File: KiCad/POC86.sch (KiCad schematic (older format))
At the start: 4 parts, among them J1 Conn_2Rows-86Pins_even_odd, J2 Conn_2Rows-86Pins_even_odd, J3 Conn_2Rows-86Pins_even_odd

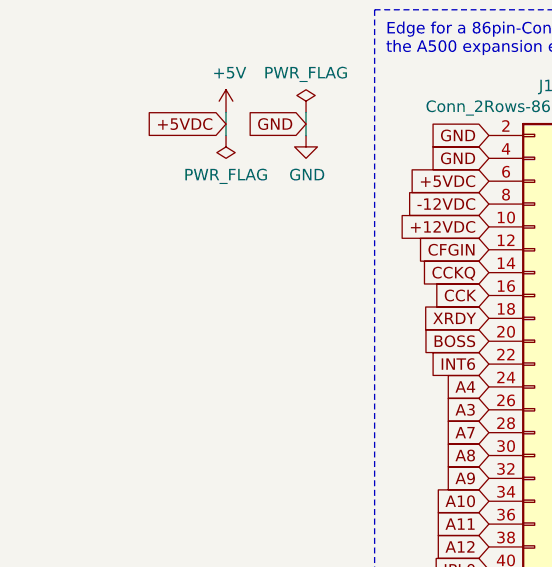
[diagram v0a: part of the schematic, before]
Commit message: added C1,C2 radial THT-capacitors for +5V-rail
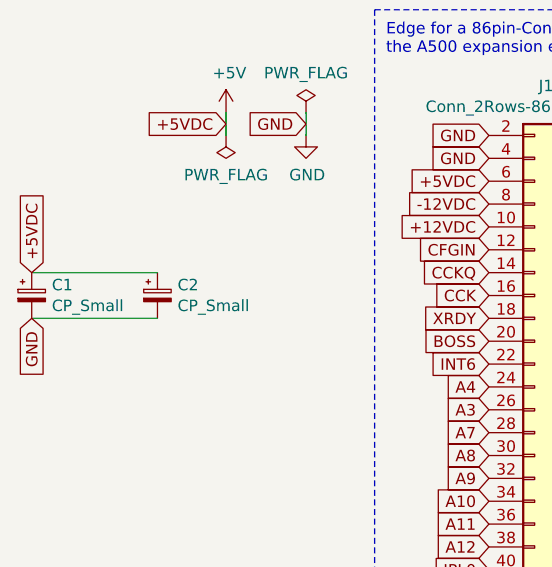
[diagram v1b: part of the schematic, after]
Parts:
- added C1, C2: CP_Small, Capacitor_THT:CP_Radial_D5.0mm_P2.50mm, symbol Device:CP_Small
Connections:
- net +5V: now also C1.1, C2.1
- net GND: now also C1.2, C2.2
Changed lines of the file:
@@
 Text Notes 5500 700  0    50   ~ 0
 New (Pass-through) expansion edge
+$Comp
+L Device:CP_Small C2
+U 1 1 628051CA
+P 1350 2250
+F 0 "C2" H 1438 2296 50  0000 L CNN
+F 1 "CP_Small" H 1438 2205 50  0000 L CNN
+F 2 "Capacitor_THT:CP_Radial_D5.0mm_P2.50mm" H 1350 2250 50  0001 C CNN
+F 3 "~" H 1350 2250 50  0001 C CNN
+	1    1350 2250
+	1    0    0    -1
+$EndComp
+$Comp
+L Device:CP_Small C1
+U 1 1 62805DF5
+P 800 2250
+F 0 "C1" H 888 2296 50  0000 L CNN
+F 1 "CP_Small" H 888 2205 50  0000 L CNN
+F 2 "Capacitor_THT:CP_Radial_D5.0mm_P2.50mm" H 800 2250 50  0001 C CNN
+F 3 "~" H 800 2250 50  0001 C CNN
+	1    800  2250
+	1    0    0    -1
+$EndComp
+Text GLabel 800  2150 1    50   Input ~ 0
++5VDC
+Wire Wire Line
+	800  2150 1350 2150
+Text GLabel 800  2350 3    50   Input ~ 0
+GND
+Wire Wire Line
+	800  2350 1350 2350
 $EndSCHEMATC

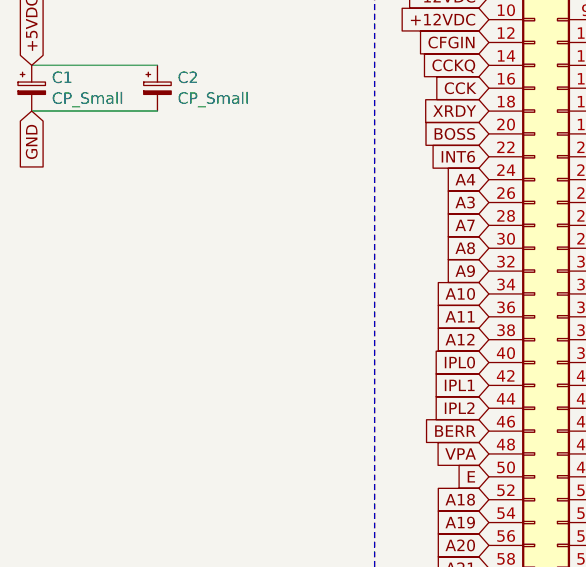
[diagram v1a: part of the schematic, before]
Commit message: added J4-pin on CFGIN-line to easily patch through this signal to J3-edge if J2-slot is empty
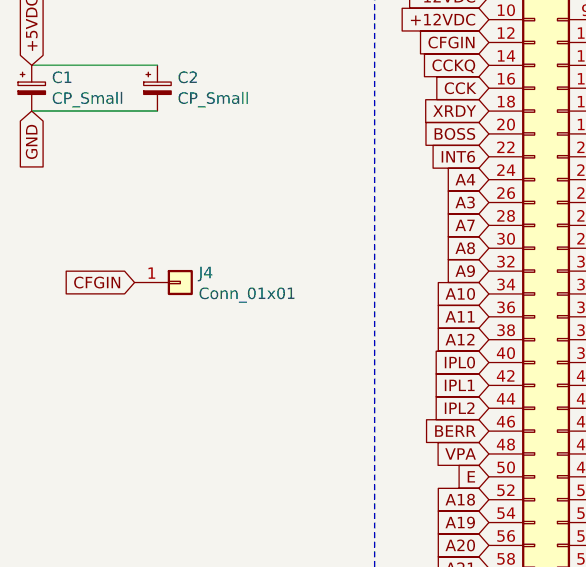
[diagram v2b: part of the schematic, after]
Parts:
- added J4: Conn_01x01, Connector_PinHeader_2.54mm:PinHeader_1x01_P2.54mm_Vertical, symbol Connector_Generic:Conn_01x01
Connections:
- net CFGIN: now also J4.1 (Pin_1)
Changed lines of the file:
@@
 Wire Wire Line
 	800  2350 1350 2350
+$Comp
+L Connector_Generic:Conn_01x01 J4
+U 1 1 62830C74
+P 1450 3100
+F 0 "J4" H 1530 3142 50  0000 L CNN
+F 1 "Conn_01x01" H 1530 3051 50  0000 L CNN
+F 2 "Connector_PinHeader_2.54mm:PinHeader_1x01_P2.54mm_Vertical" H 1450 3100 50  0001 C CNN
+F 3 "~" H 1450 3100 50  0001 C CNN
+	1    1450 3100
+	1    0    0    -1
+$EndComp
+Text GLabel 1250 3100 0    50   Input ~ 0
+CFGIN
 $EndSCHEMATC

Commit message: Redesign to a more Compact Edition with no pass-through expansion edge
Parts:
- removed J3: Conn_2Rows-86Pins_even_odd, POC86:A500_86pin_Edge_Connector, symbol POC86:Conn_2Rows-86Pins_even_odd
- removed J4: Conn_01x01, Connector_PinHeader_2.54mm:PinHeader_1x01_P2.54mm_Vertical, symbol Connector_Generic:Conn_01x01
- removed JP1: Jumper_2_Open, Connector_PinHeader_2.54mm:PinHeader_1x02_P2.54mm_Vertical, symbol Jumper:Jumper_2_Open
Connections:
- net CFGOUT: now also J2.11 (Pin_11)
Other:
- note added: "86pin-Connector"
- note removed: "86pin-Connector in the Middle"
- note removed: "New (Pass-through) expansion edge"
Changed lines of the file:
@@
 Text GLabel 2000 1500 0    50   Input ~ 0
 GND
-Text GLabel 6250 1550 2    50   Input ~ 0
-GND
-Text GLabel 6250 1650 2    50   Input ~ 0
-GND
-Text GLabel 6250 1750 2    50   Input ~ 0
-+5VDC
-Text GLabel 6250 1850 2    50   Input ~ 0
-CLK7M
-Text GLabel 5750 1550 0    50   Input ~ 0
-GND
-Text GLabel 5750 1650 0    50   Input ~ 0
-GND
-Text GLabel 5750 1750 0    50   Input ~ 0
-+5VDC
-Text GLabel 5750 1850 0    50   Input ~ 0
--12VDC
-Text GLabel 6250 1950 2    50   Input ~ 0
-CLK28M
-Text GLabel 5750 1950 0    50   Input ~ 0
-+12VDC
-Text GLabel 6250 2150 2    50   Input ~ 0
-GND
-Text GLabel 5750 2150 0    50   Input ~ 0
-CCKQ
-Text GLabel 6250 2250 2    50   Input ~ 0
-CDAC
-Text GLabel 5750 2250 0    50   Input ~ 0
-CCK
-Text GLabel 6250 2350 2    50   Input ~ 0
-OVR
-Text GLabel 5750 2350 0    50   Input ~ 0
-XRDY
-Text GLabel 6250 2450 2    50   Input ~ 0
-INT2
-Text GLabel 5750 2450 0    50   Input ~ 0
-BOSS
-Text GLabel 6250 2550 2    50   Input ~ 0
-A5
-Text GLabel 5750 2550 0    50   Input ~ 0
-INT6
-Text GLabel 6250 2650 2    50   Input ~ 0
-A6
-Text GLabel 5750 2650 0    50   Input ~ 0
-A4
-Text GLabel 6250 2750 2    50   Input ~ 0
-GND
-Text GLabel 5750 2750 0    50   Input ~ 0
-A3
-Text GLabel 6250 2850 2    50   Input ~ 0
-A2
-Text GLabel 5750 2850 0    50   Input ~ 0
-A7
-Text GLabel 6250 2950 2    50   Input ~ 0
-A1
-Text GLabel 5750 2950 0    50   Input ~ 0
-A8
-Text GLabel 6250 3050 2    50   Input ~ 0
-FC0
-Text GLabel 5750 3050 0    50   Input ~ 0
-A9
-Text GLabel 6250 3150 2    50   Input ~ 0
-FC1
-Text GLabel 5750 3150 0    50   Input ~ 0
-A10
-Text GLabel 6250 3250 2    50   Input ~ 0
-FC2
-Text GLabel 5750 3250 0    50   Input ~ 0
-A11
-Text GLabel 6250 3350 2    50   Input ~ 0
-GND
-Text GLabel 5750 3350 0    50   Input ~ 0
-A12
-Text GLabel 6250 3450 2    50   Input ~ 0
-A13
-Text GLabel 5750 3450 0    50   Input ~ 0
-IPL0
-Text GLabel 6250 3550 2    50   Input ~ 0
-A14
-Text GLabel 5750 3550 0    50   Input ~ 0
-IPL1
-Text GLabel 6250 3650 2    50   Input ~ 0
-A15
-Text GLabel 5750 3650 0    50   Input ~ 0
-IPL2
-Text GLabel 6250 3750 2    50   Input ~ 0
-A16
-Text GLabel 5750 3750 0    50   Input ~ 0
-BERR
-Text GLabel 6250 3850 2    50   Input ~ 0
-A17
-Text GLabel 5750 3850 0    50   Input ~ 0
-VPA
-Text GLabel 6250 3950 2    50   Input ~ 0
-GND
-Text GLabel 5750 3950 0    50   Input ~ 0
-E
-Text GLabel 6250 4050 2    50   Input ~ 0
-VMA
-Text GLabel 5750 4050 0    50   Input ~ 0
-A18
-Text GLabel 6250 4150 2    50   Input ~ 0
-RST
-Text GLabel 5750 4150 0    50   Input ~ 0
-A19
-Text GLabel 6250 4250 2    50   Input ~ 0
-HLT
-Text GLabel 5750 4250 0    50   Input ~ 0
-A20
-Text GLabel 6250 4350 2    50   Input ~ 0
-A22
-Text GLabel 5750 4350 0    50   Input ~ 0
-A21
-Text GLabel 6250 4450 2    50   Input ~ 0
-A23
-Text GLabel 5750 4450 0    50   Input ~ 0
-BR
-Text GLabel 6250 4550 2    50   Input ~ 0
-GND
-Text GLabel 5750 4550 0    50   Input ~ 0
-BGACK
-Text GLabel 6250 4650 2    50   Input ~ 0
-D15
-Text GLabel 5750 4650 0    50   Input ~ 0
-BG
-Text GLabel 6250 4750 2    50   Input ~ 0
-D14
-Text GLabel 5750 4750 0    50   Input ~ 0
-DTACK
-Text GLabel 6250 4850 2    50   Input ~ 0
-D13
-Text GLabel 5750 4850 0    50   Input ~ 0
-RW
-Text GLabel 6250 4950 2    50   Input ~ 0
-D12
-Text GLabel 5750 4950 0    50   Input ~ 0
-LDS
-Text GLabel 6250 5050 2    50   Input ~ 0
-D11
-Text GLabel 5750 5050 0    50   Input ~ 0
-UDS
-Text GLabel 6250 5150 2    50   Input ~ 0
-GND
-Text GLabel 5750 5150 0    50   Input ~ 0
-AS
-Text GLabel 6250 5250 2    50   Input ~ 0
-D0
-Text GLabel 5750 5250 0    50   Input ~ 0
-D10
-Text GLabel 6250 5350 2    50   Input ~ 0
-D1
-Text GLabel 5750 5350 0    50   Input ~ 0
-D9
-Text GLabel 6250 5450 2    50   Input ~ 0
-D2
-Text GLabel 5750 5450 0    50   Input ~ 0
-D8
-Text GLabel 6250 5550 2    50   Input ~ 0
-D3
-Text GLabel 5750 5550 0    50   Input ~ 0
-D7
-Text GLabel 6250 5650 2    50   Input ~ 0
-D4
-Text GLabel 5750 5650 0    50   Input ~ 0
-D6
-Text GLabel 6250 5750 2    50   Input ~ 0
-GND
-Text GLabel 5750 5750 0    50   Input ~ 0
-D5
 Text GLabel 3300 1550 2    50   Input ~ 0
 GND
@@
 	1    0    0    -1
 $EndComp
-$Comp
-L POC86:Conn_2Rows-86Pins_even_odd J3
-U 1 1 5FD12767
-P 6000 3650
-F 0 "J3" H 6000 5967 50  0000 C CNN
-F 1 "Conn_2Rows-86Pins_even_odd" H 6000 5876 50  0000 C CNN
-F 2 "POC86:A500_86pin_Edge_Connector" H 5950 3950 50  0001 C CNN
-F 3 "~" H 5950 3950 50  0001 C CNN
-	1    6000 3650
-	1    0    0    -1
-$EndComp
 Text GLabel 4800 1550 2    50   Input ~ 0
 GND
@@
 Text GLabel 4800 2150 2    50   Input ~ 0
 GND
-Text GLabel 6750 2050 2    50   Input ~ 0
+Text GLabel 4800 2050 2    50   Input ~ 0
 CFGOUT
 Text GLabel 4300 2150 0    50   Input ~ 0
@@
 Text GLabel 3300 2050 2    50   Input ~ 0
 CFGOUT
-Wire Wire Line
-	4800 2050 5300 2050
-$Comp
-L Jumper:Jumper_2_Open JP1
-U 1 1 6267DA04
-P 6000 1100
-F 0 "JP1" H 6000 1335 50  0000 C CNN
-F 1 "Jumper_2_Open" H 6000 1244 50  0000 C CNN
-F 2 "Connector_PinHeader_2.54mm:PinHeader_1x02_P2.54mm_Vertical" H 6000 1100 50  0001 C CNN
-F 3 "~" H 6000 1100 50  0001 C CNN
-	1    6000 1100
-	1    0    0    -1
-$EndComp
-Wire Wire Line
-	5300 2050 5300 1100
-Wire Wire Line
-	5300 1100 5800 1100
-Connection ~ 5300 2050
-Wire Wire Line
-	5300 2050 5750 2050
-Wire Wire Line
-	6200 1100 6750 1100
-Wire Wire Line
-	6750 1100 6750 2050
-Wire Wire Line
-	6750 2050 6250 2050
 Wire Notes Line
 	2300 1000 3800 1000
@@
 Wire Notes Line
 	3900 6150 3900 1000
-Text Notes 3950 1150 0    50   ~ 0
-86pin-Connector in the Middle
-Wire Notes Line
-	5350 550  5350 6150
-Wire Notes Line
-	5350 6150 7250 6150
-Wire Notes Line
-	7250 6150 7250 550
-Wire Notes Line
-	7250 550  5350 550
-Text Notes 5500 700  0    50   ~ 0
-New (Pass-through) expansion edge
+Text Notes 4200 1150 0    50   ~ 0
+86pin-Connector
 $Comp
 L Device:CP_Small C2
@@
 Wire Wire Line
 	800  2350 1350 2350
-$Comp
-L Connector_Generic:Conn_01x01 J4
-U 1 1 62830C74
-P 1450 3100
-F 0 "J4" H 1530 3142 50  0000 L CNN
-F 1 "Conn_01x01" H 1530 3051 50  0000 L CNN
-F 2 "Connector_PinHeader_2.54mm:PinHeader_1x01_P2.54mm_Vertical" H 1450 3100 50  0001 C CNN
-F 3 "~" H 1450 3100 50  0001 C CNN
-	1    1450 3100
-	1    0    0    -1
-$EndComp
-Text GLabel 1250 3100 0    50   Input ~ 0
-CFGIN
 $EndSCHEMATC
